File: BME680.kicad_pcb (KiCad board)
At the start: 2 copper layers, 25.4 x 17.8 mm, 26 parts, among them IC1 BME680, Q2 BSS138, U2 AP2112K-3.3

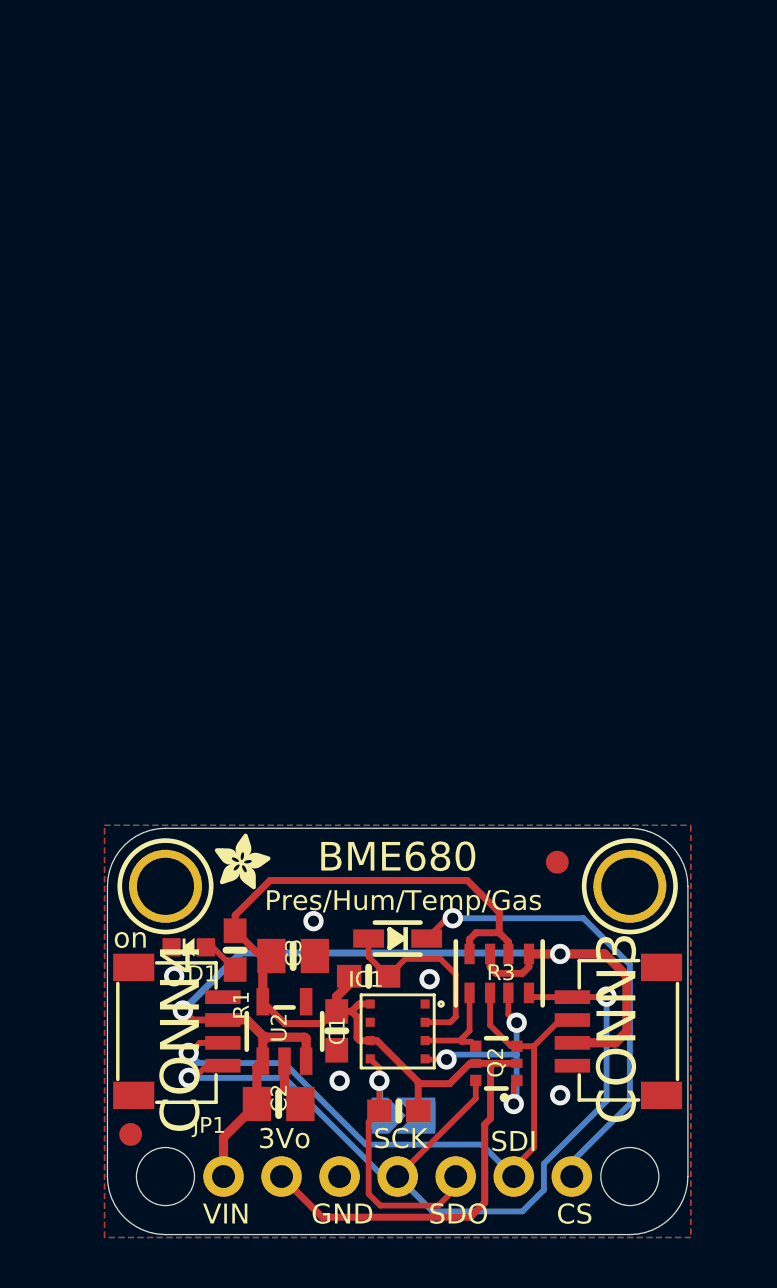
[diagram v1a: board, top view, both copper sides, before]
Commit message: update BME680 scheme
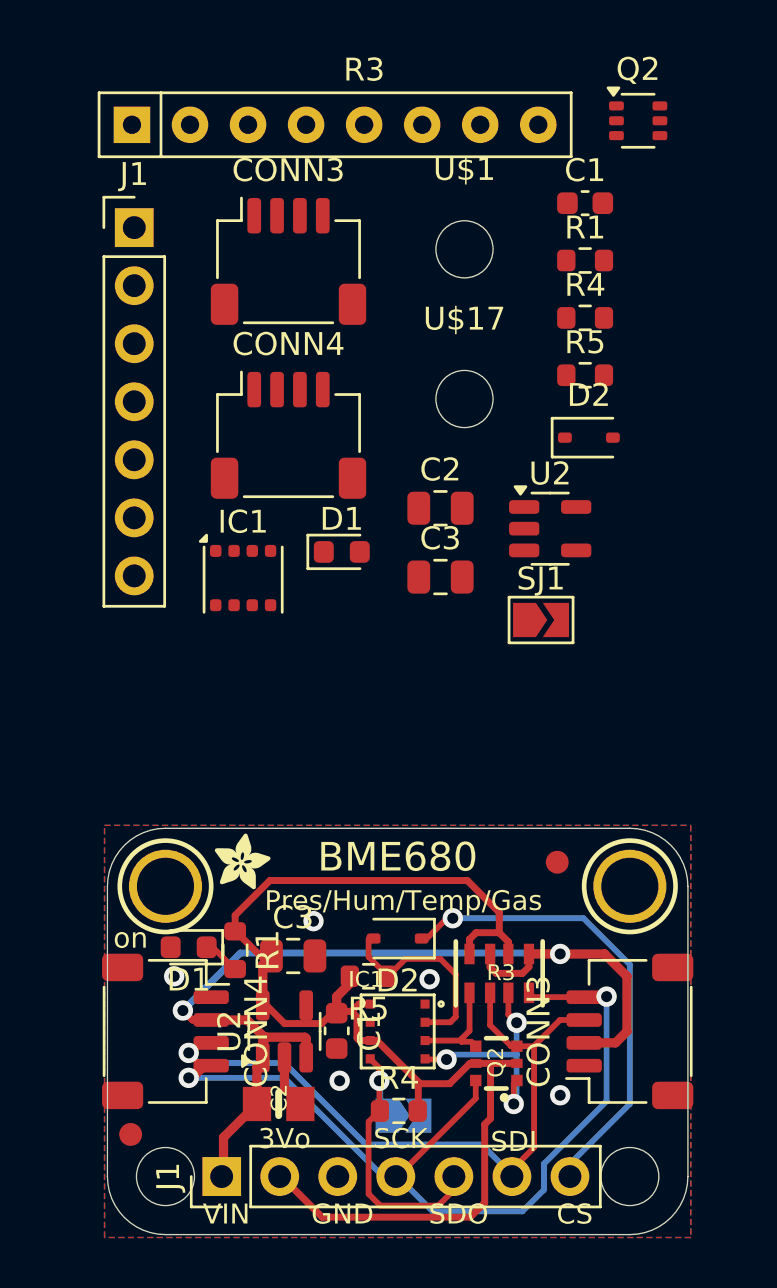
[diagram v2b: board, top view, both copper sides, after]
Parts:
- added C1: 0.1uF, Capacitor_SMD:C_0603_1608Metric, F.Cu at (156.7, 68.8)
- added C2: 10uF, Capacitor_SMD:C_0805_2012Metric, F.Cu at (150.4, 82.1)
- added C3: 10uF, Capacitor_SMD:C_0805_2012Metric, F.Cu at (150.4, 85.1)
- added CONN3: STEMMA_I2C_QT, Connector_JST:JST_SH_SM04B-SRSS-TB_1x04-1MP_P1.00mm_Horizontal, F.Cu at (143.7, 71.3)
- added CONN4: STEMMA_I2C_QT, Connector_JST:JST_SH_SM04B-SRSS-TB_1x04-1MP_P1.00mm_Horizontal, F.Cu at (143.7, 78.9)
- added D1: GREEN, LED_SMD:LED_0603_1608Metric, F.Cu at (146.1, 84.0)
- added D2: 1N4148, Diode_SMD:D_SOD-323, F.Cu at (156.9, 79.0)
- added IC1: BME680, Package_LGA:Bosch_LGA-8_3x3mm_P0.8mm_ClockwisePinNumbering, F.Cu at (141.7, 85.2)
- added J1: HEADER-1X770MIL, Connector_PinHeader_2.54mm:PinHeader_1x07_P2.54mm_Vertical, F.Cu at (137.0, 69.8)
- added Q2: BSS138, Package_TO_SOT_SMD:SOT-363_SC-70-6, F.Cu at (159.0, 65.2)
- added R1: 10K, Resistor_SMD:R_0603_1608Metric, F.Cu at (156.7, 71.3)
- added R3: 10K, Resistor_THT:R_Array_SIP8, F.Cu at (136.9, 65.3)
- added R4: 10K, Resistor_SMD:R_0603_1608Metric, F.Cu at (156.7, 73.8)
- added R5: 10K, Resistor_SMD:R_0603_1608Metric, F.Cu at (156.7, 76.3)
- added SJ1: SOLDERJUMPER, Jumper:SolderJumper-2_P1.3mm_Open_TrianglePad1.0x1.5mm, F.Cu at (154.8, 87.0)
- added U$1: MOUNTINGHOLE2.5, MountingHole:MountingHole_2.5mm, F.Cu at (151.4, 70.8)
- added U$17: MOUNTINGHOLE2.5, MountingHole:MountingHole_2.5mm, F.Cu at (151.4, 77.3)
- added U2: AP2112K-3.3, Package_TO_SOT_SMD:SOT-23-5, F.Cu at (155.2, 83.0)
- C1: footprint 0603-NO -> Capacitor_SMD:C_0603_1608Metric
- C3: footprint 0805-NO -> Capacitor_SMD:C_0805_2012Metric
- CONN3, CONN4: footprint JST_SH4 -> Connector_JST:JST_SH_SM04B-SRSS-TB_1x04-1MP_P1.00mm_Horizontal
- D1: footprint CHIPLED_0603_NOOUTLINE -> LED_SMD:LED_0603_1608Metric
- D2: footprint SOD-323 -> Diode_SMD:D_SOD-323
- J1: renamed from JP1; footprint 1X07_ROUND_70 -> Connector_PinHeader_2.54mm:PinHeader_1x07_P2.54mm_Vertical
- R1, R4, R5: footprint 0603-NO -> Resistor_SMD:R_0603_1608Metric
- SJ1: footprint SOLDERJUMPER_ARROW_NOPASTE -> Jumper:SolderJumper-2_P1.3mm_Open_TrianglePad1.0x1.5mm
- U2: footprint SOT23-5 -> Package_TO_SOT_SMD:SOT-23-5
- moved J1 7.70 mm to (140.8, 111.4), turned to 90 degrees
- turned D1 to 180 degrees
- turned U2 to 90 degrees

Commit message: update BME680 routing and footprints
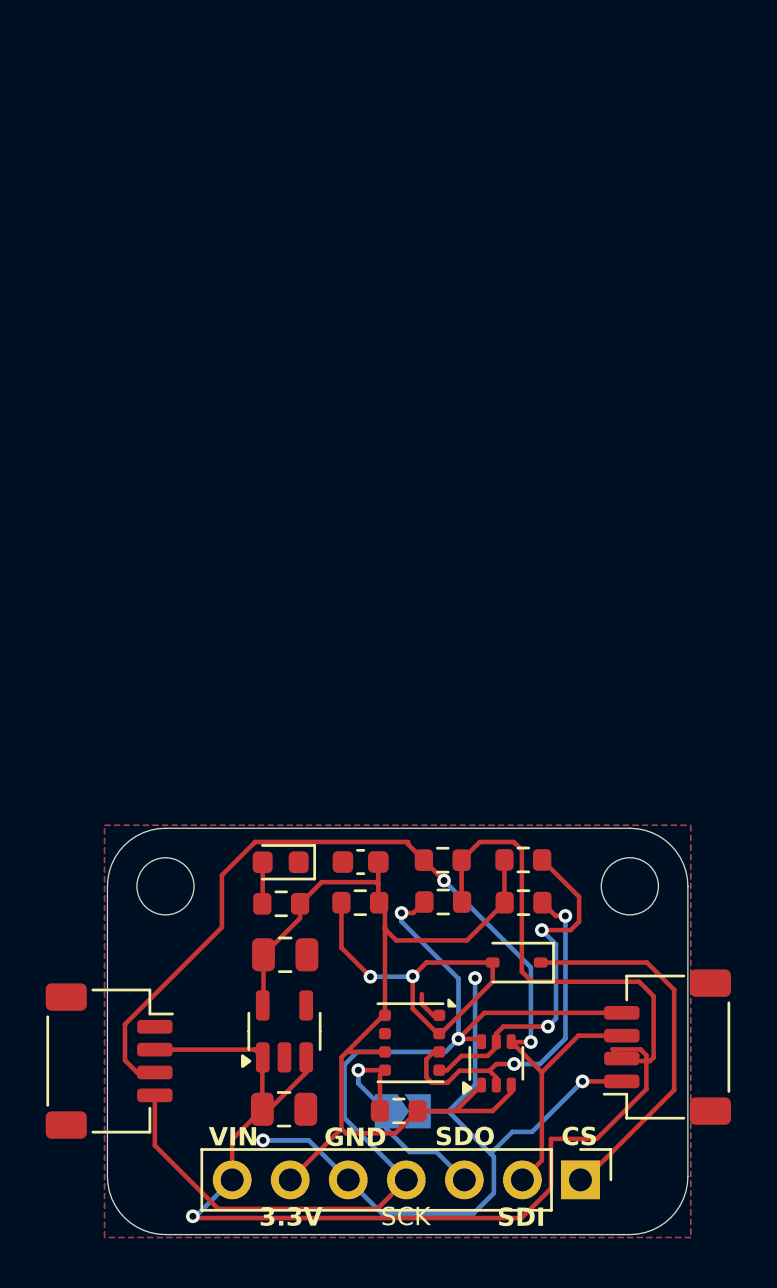
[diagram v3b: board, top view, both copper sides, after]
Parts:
- removed @HOLE0, @HOLE1: , 
- removed the C1 at (156.7, 68.8)
- removed the C2 at (150.4, 82.1)
- removed the C3 at (150.4, 85.1)
- removed the CONN3 at (158.7, 105.0)
- removed the CONN3 at (143.7, 71.3)
- removed the CONN4 at (143.7, 78.9)
- removed the D1 at (146.1, 84.0)
- removed the D2 at (156.9, 79.0)
- removed FID3, FID4: FIDUCIAL_1MM, FIDUCIAL_1MM
- removed the IC1 at (141.7, 85.2)
- removed the J1 at (137.0, 69.8)
- removed the Q2 at (159.0, 65.2)
- removed the R1 at (156.7, 71.3)
- removed the R3 at (152.9, 102.5)
- removed the R3 at (136.9, 65.3)
- removed the R4 at (156.7, 73.8)
- removed the R5 at (156.7, 76.3)
- removed the SJ1 at (154.8, 87.0)
- removed the U$1 at (151.4, 70.8)
- removed the U$17 at (151.4, 77.3)
- removed U$25: , PCBFEAT-REV-040
- removed U$30, U$31: , STEMMAQT
- removed U$4: , ADAFRUIT_2.5MM
- removed the U2 at (155.2, 83.0)
- added CONN3: STEMMA_I2C_QT, Connector_JST:JST_SH_SM04B-SRSS-TB_1x04-1MP_P1.00mm_Horizontal, F.Cu at (160.3, 105.7)
- added R2: 10k, Resistor_SMD:R_0603_1608Metric, F.Cu at (150.5, 99.3)
- added R3: 10k, Resistor_SMD:R_0603_1608Metric, F.Cu at (150.5, 97.5)
- added R6: 10k, Resistor_SMD:R_0603_1608Metric, F.Cu at (154.0, 97.5)
- added R7: 10k, Resistor_SMD:R_0603_1608Metric, F.Cu at (154.0, 99.4)
- C2: footprint 0805-NO -> Capacitor_SMD:C_0805_2012Metric
- IC1: footprint BME680 -> Package_LGA:Bosch_LGA-8_3x3mm_P0.8mm_ClockwisePinNumbering
- J1: value (none) -> HEADER-1X770MIL
- Q2: footprint SOT363 -> Package_TO_SOT_SMD:SOT-363_SC-70-6
- SJ1: value (none) -> SOLDERJUMPER
- U$1, U$17: footprint MOUNTINGHOLE_2.5_PLATED -> MountingHole:MountingHole_2.5mm
- moved J1 15.7 mm to (156.5, 111.5), turned to -90 degrees
- moved C1 7.46 mm to (146.9, 97.6), turned to 180 degrees
- moved D1 5.48 mm to (143.4, 97.6)
- moved D2 5.31 mm to (153.7, 102.0)
- moved R5 3.24 mm to (146.9, 99.4), turned to 0 degrees
- moved R1 2.86 mm to (143.4, 99.4), turned to 180 degrees
- moved CONN4 2.79 mm to (135.9, 106.3)
- moved IC1 0.80 mm to (149.1, 105.5), turned to -90 degrees
- moved C3 0.35 mm to (143.6, 101.7)
- moved C2 0.33 mm to (143.5, 108.4)
- moved SJ1 0.19 mm to (148.7, 108.5)
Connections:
- CONN4 pad 3: SDI/SDA -> /SDI/SDA
- CONN4 pad 4: SCK/SCL -> /SCK/SCL
- D1 pad 1: (no net) -> GND
- D1 pad 2: (no net) -> Net-(D1-A)
- D2 pad 1: (no net) -> /CS
- D2 pad 2: (no net) -> /CS_3V
- IC1 pad 2: CS_3V -> /CS_3V
- IC1 pad 3: SDI_3V -> /SDI_3V
- IC1 pad 4: SCK_3V -> /SCK_3V
- IC1 pad 5: SDO/ADR -> /SDO/ADR
- IC1 pad 7: GND -> unconnected-(IC1-GND-Pad7)
- J1 pad 1: VCC -> /CS
- J1 pad 2: 3.3V -> /SDI/SDA
- J1 pad 3: GND -> /SDO/ADR
- J1 pad 4: SCK/SCL -> /SCK/SCL
- J1 pad 5: SDO/ADR -> GND
- J1 pad 6: SDI/SDA -> 3.3V
- J1 pad 7: CS -> VCC
- Q2 pad 1: SCK_3V -> 3.3V
- Q2 pad 2: 3.3V -> /SDI_3V
- Q2 pad 3: SDI/SDA -> 3.3V
- Q2 pad 4: SDI_3V -> /SDI/SDA
- Q2 pad 5: 3.3V -> /SCK_3V
- Q2 pad 6: SCK/SCL -> /SCK/SCL
- R1 pad 2: N$1 -> Net-(D1-A)
- R4 pad 1: SDO/ADR -> /SDO/ADR
- R5 pad 1: CS_3V -> /CS_3V
- SJ1 pad 1: SDO/ADR -> /SDO/ADR
- U2 pad 4: (no net) -> unconnected-(U2-NC-Pad4)
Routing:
- net /SDI/SDA: track 0.00 -> 43.1 mm, vias 0 -> 2
- net /SCK/SCL: track 0.00 -> 42.9 mm, vias 0 -> 2
- net SCK/SCL: track 38.8 -> 0.00 mm, vias 2 -> 0
- net SDI/SDA: track 30.1 -> 0.00 mm, vias 1 -> 0
- net GND: track 2.16 -> 32.2 mm, vias 5 -> 3
- net CS: track 20.4 -> 0.00 mm, vias 1 -> 0
- net VCC: track 44.2 -> 63.3 mm, vias 2 -> 1
- net /CS_3V: track 0.00 -> 16.5 mm, vias 0 -> 2
- net /CS: track 0.00 -> 16.5 mm
- net /SDI_3V: track 0.00 -> 15.8 mm, vias 0 -> 2
- net /SCK_3V: track 0.00 -> 15.7 mm, vias 0 -> 2
- net SDO/ADR: track 12.7 -> 0.00 mm, vias 1 -> 0
- net 3.3V: track 55.7 -> 44.4 mm
- net /SDO/ADR: track 0.00 -> 10.5 mm, vias 0 -> 1
- net SCK_3V: track 10.3 -> 0.00 mm, vias 3 -> 0
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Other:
- board text added: "3.3V"
- board text removed: "3Vo"
- board text removed: "Addr"
- board text removed: "BME680"
- board text removed: "Default I2C Addr 0x77"
- board text removed: "Pres/Hum/Temp/Gas"
- board text removed: "Temp, Pressure Humidity & Gas"
- board text removed: "VLogic/Vcc: 3-5VDC"
- board text removed: "on"

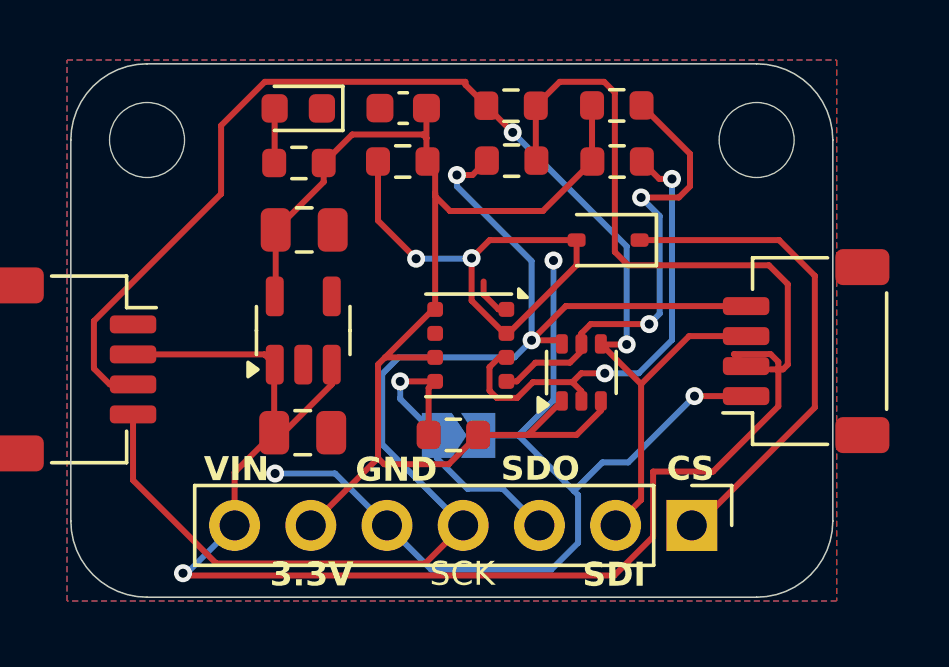
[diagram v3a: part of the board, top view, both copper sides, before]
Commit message: minor fixes in silkscreen and schematic layout
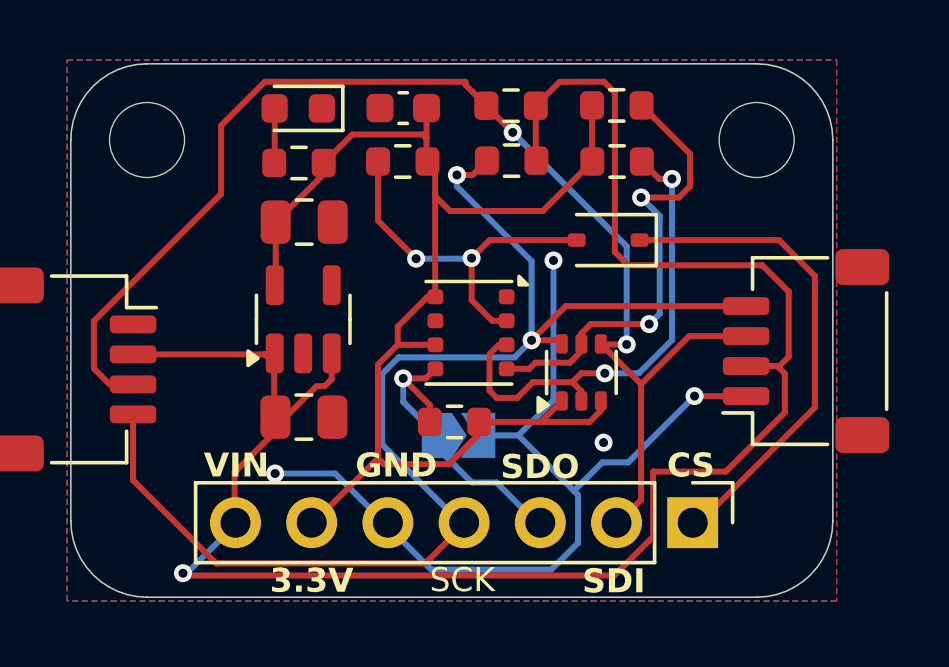
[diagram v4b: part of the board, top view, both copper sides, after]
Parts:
- moved C2 0.52 mm to (143.6, 107.9)
- moved R4 0.44 mm to (148.6, 108.0)
- moved IC1 0.42 mm to (149.1, 105.1)
- moved U2 0.37 mm to (143.5, 104.6)
- moved C3 0.26 mm to (143.6, 101.4)
- moved J1 0.09 mm to (156.5, 111.4)
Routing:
- net /CS_3V: track 16.5 -> 12.2 mm
- net GND: track 32.2 -> 30.8 mm, vias 3 -> 4
- net VCC: track 63.3 -> 62.3 mm
- net 3.3V: track 44.4 -> 43.7 mm

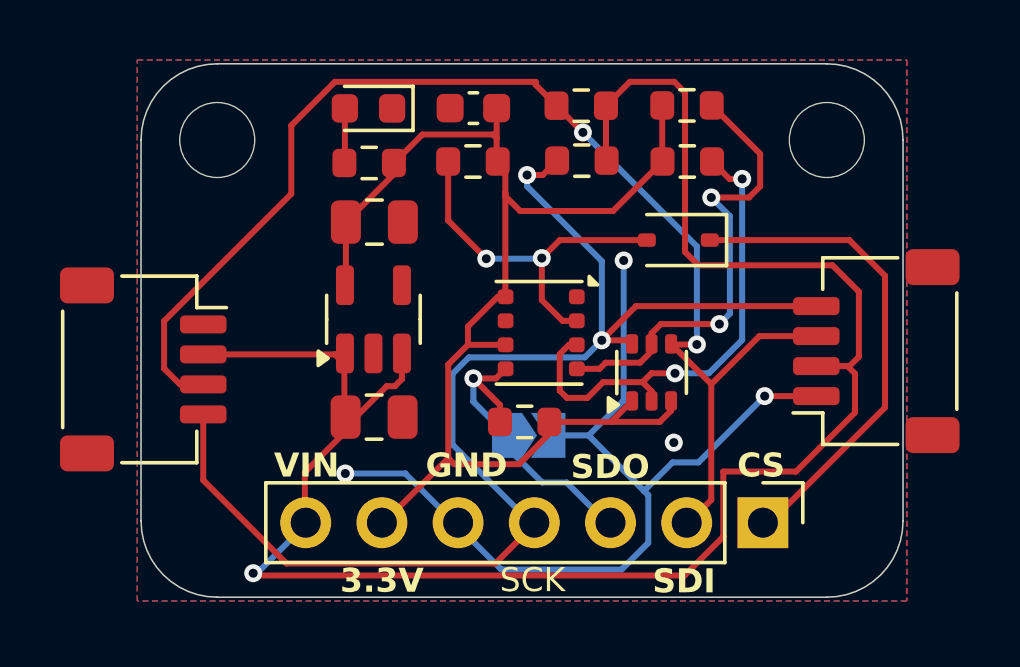
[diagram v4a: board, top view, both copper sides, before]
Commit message: routing done with freerouting + delete stemma connectors
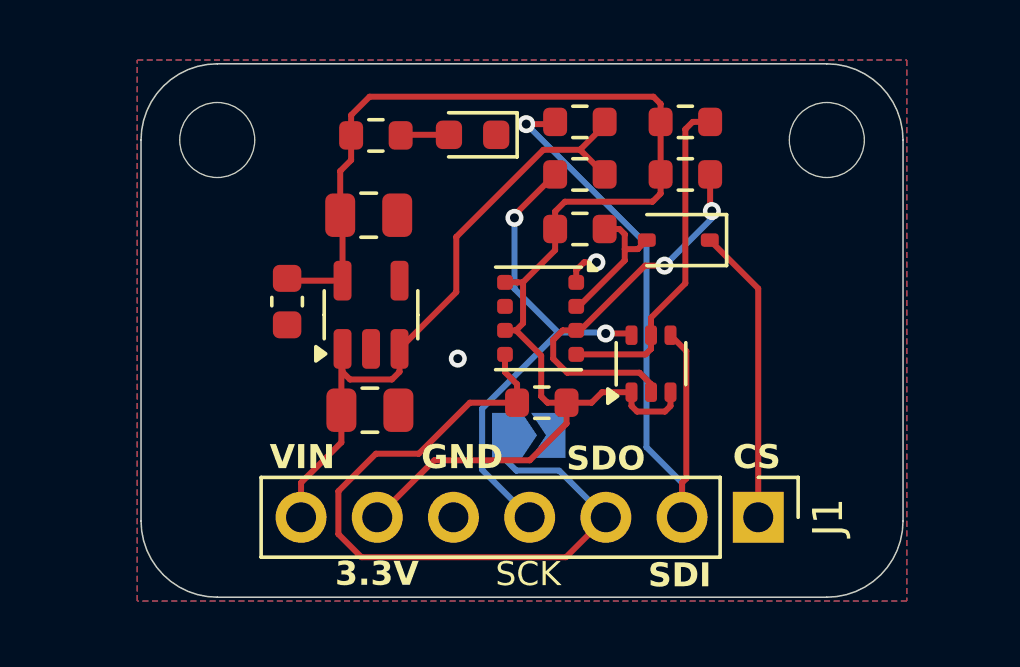
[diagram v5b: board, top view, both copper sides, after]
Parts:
- removed CONN3, CONN4: STEMMA_I2C_QT, Connector_JST:JST_SH_SM04B-SRSS-TB_1x04-1MP_P1.00mm_Horizontal
- moved C1 8.95 mm to (140.7, 104.0), turned to -90 degrees
- moved R5 4.22 mm to (150.4, 101.6), turned to 180 degrees
- moved D1 3.58 mm to (146.9, 98.5)
- moved R1 0.95 mm to (143.6, 98.5), turned to 0 degrees
- moved R4 0.86 mm to (149.2, 107.4)
- moved R6 0.55 mm to (153.9, 98.0)
- moved R3 0.54 mm to (150.4, 98.0)
- moved IC1 0.48 mm to (149.1, 104.6)
- moved R2 0.46 mm to (150.4, 99.8)
- moved R7 0.43 mm to (153.9, 99.8)
- moved C3 0.30 mm to (143.4, 101.2)
- moved Q2 0.29 mm to (152.8, 106.1)
- moved C2 0.27 mm to (143.4, 107.7)
- moved J1 0.24 mm to (156.4, 111.2)
- moved U2 0.17 mm to (143.5, 104.5)
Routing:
- net VCC: track 62.3 -> 22.1 mm, vias 1 -> 0
- net GND: track 30.8 -> 1.19 mm, vias 4 -> 2
- net /SCK/SCL: track 42.9 -> 16.8 mm
- net /SDI/SDA: track 43.1 -> 22.6 mm, vias 2 -> 1
- net /SDO/ADR: track 10.3 -> 25.1 mm, vias 1 -> 0
- net /CS_3V: track 12.2 -> 4.73 mm, vias 2 -> 0
- net /CS: track 16.5 -> 9.91 mm
- net /SCK_3V: track 15.5 -> 11.3 mm, vias 2 -> 0
- net /SDI_3V: track 16.3 -> 13.0 mm
- net 3.3V: track 43.7 -> 46.9 mm
